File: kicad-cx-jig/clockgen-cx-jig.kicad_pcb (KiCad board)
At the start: 2 copper layers, 20.2 x 12 mm, 10 parts, among them J1 Conn_Coaxial, J2 Conn_01x01_Pin, J3 Conn_01x01_Pin, J4 Conn_01x01_Pin, J5 Conn_01x01_Pin

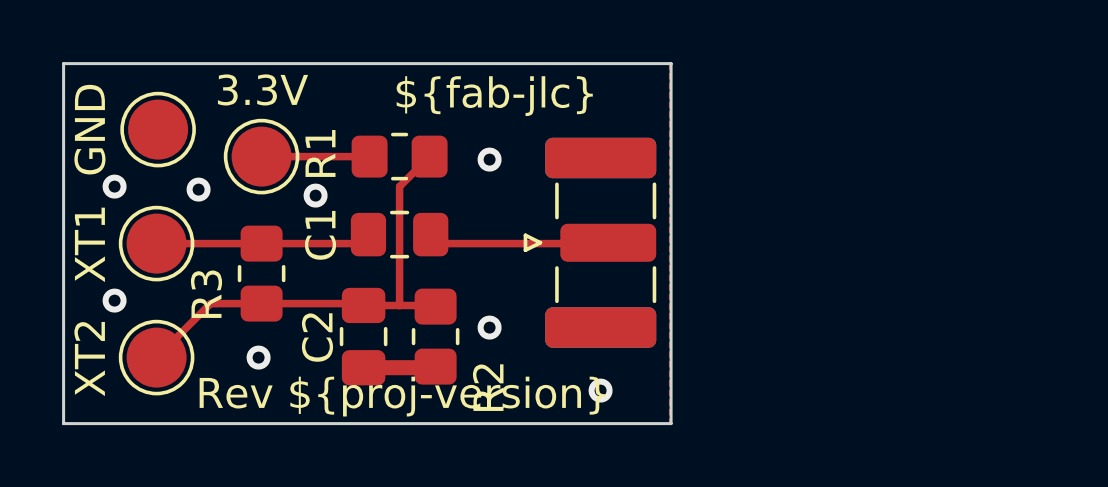
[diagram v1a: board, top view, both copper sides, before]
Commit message: Add initial fp-lib-table and sym-lib-table for KiCad project
- Created fp-lib-table with version 7 for footprint libraries.
- Created sym-lib-table with version 7 for symbol libraries.
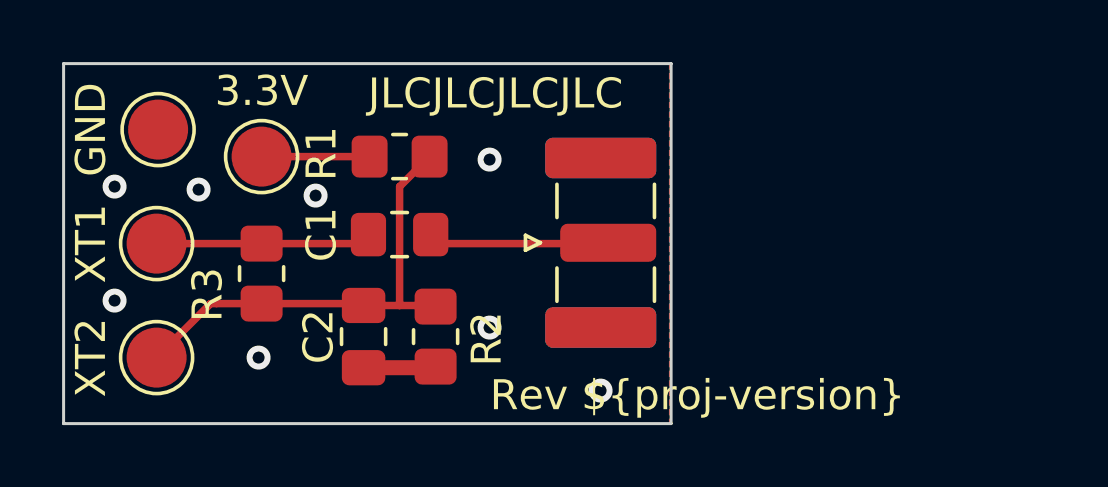
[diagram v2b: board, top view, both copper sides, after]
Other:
- board text added: "JLCJLCJLCJLC"
- board text removed: "${ISSUE_DATE}"
- board text removed: "${TITLE}"
- board text removed: "${fab-jlc}"
- board text removed: "${proj-author} ${proj-license}"
